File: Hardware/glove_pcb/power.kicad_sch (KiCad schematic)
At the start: 21 parts, among them J1 3551, J2 OSTVN02A150, J3 54-00130, U1 AP63205WU, U2 TCR2EF33_LMCT

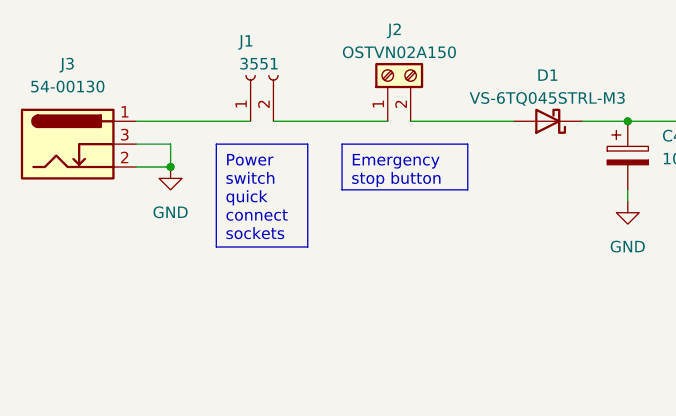
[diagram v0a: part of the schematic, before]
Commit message: Assign footprints and import all parts into pcb editor
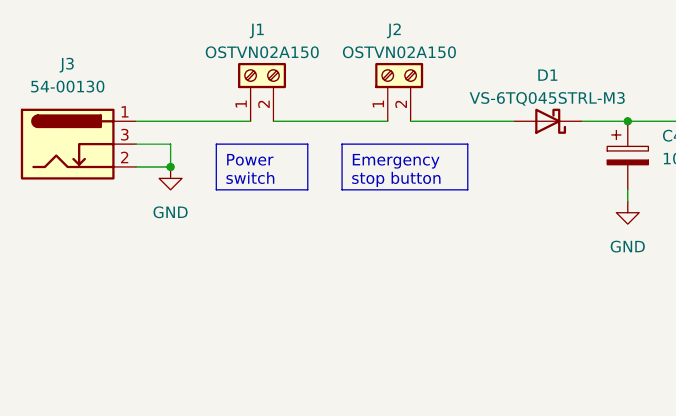
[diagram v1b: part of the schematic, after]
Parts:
- J1: value 3551 -> OSTVN02A150; footprint (none) -> Glove_Footprints:TerminalBlock_OnShore_OSTVN02A150_P2.54mm; symbol Connector:Conn_01x02_Socket -> Connector:Screw_Terminal_01x02
- J2: footprint (none) -> Glove_Footprints:TerminalBlock_OnShore_OSTVN02A150_P2.54mm

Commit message: Re-placing with new outline
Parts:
- L1: footprint Inductor_SMD:L_0805_2012Metric_Pad1.05x1.20mm_HandSolder -> Glove_Footprints:L_7.6x7.6_H3.5
